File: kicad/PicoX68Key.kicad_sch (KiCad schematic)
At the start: 20 parts, among them J1 TO_X68000, Q1 2N7000, Q2 2N7000, Q3 2N7000, U1 Pico

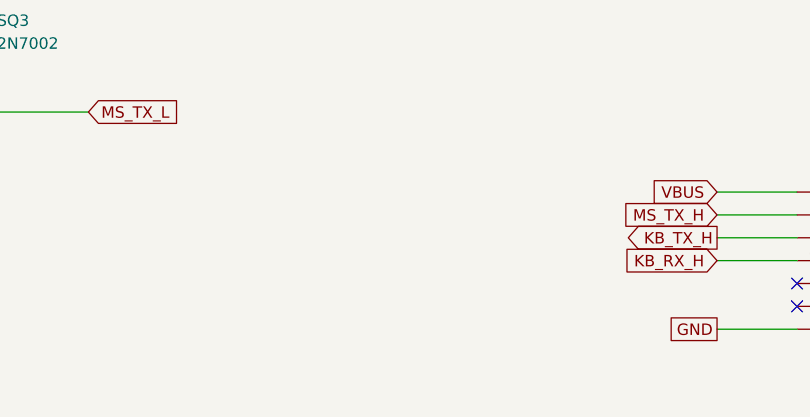
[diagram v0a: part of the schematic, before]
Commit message: Add mini-din7 connector, finish routing
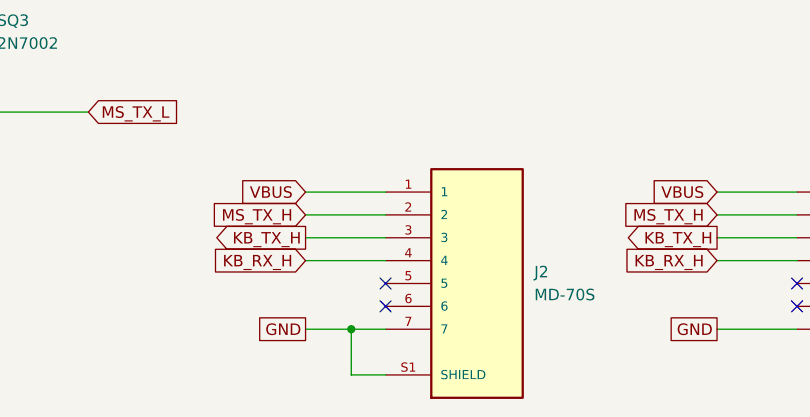
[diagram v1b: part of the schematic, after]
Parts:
- added J2: MD-70S, Library:CUI_MD-70S, symbol Library:MD-70S
- J1: footprint Connector_PinSocket_2.54mm:PinSocket_1x07_P2.54mm_Horizontal -> Connector_PinSocket_2.54mm:PinSocket_1x07_P2.54mm_Vertical
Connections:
- net GND: now also J2.7, J2.S1 (SHIELD)
- net KB_RX_H: now also J2.4
- net KB_TX_H: now also J2.3
- net MS_TX_H: now also J2.2
- net VBUS: now also J2.1
- no-connect marks 30 -> 32

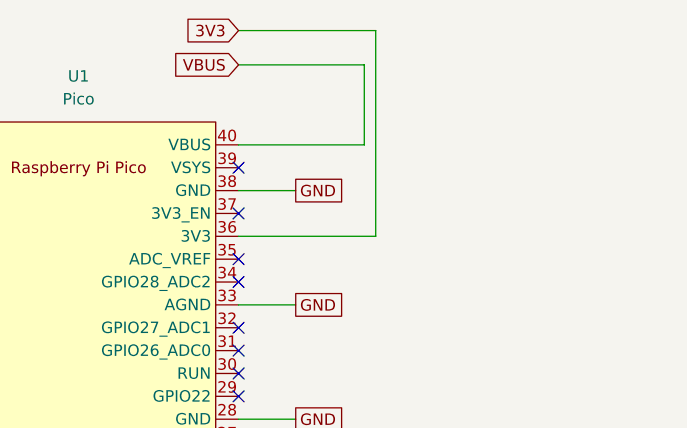
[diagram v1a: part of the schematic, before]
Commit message: Layout tidy up, add flood planes
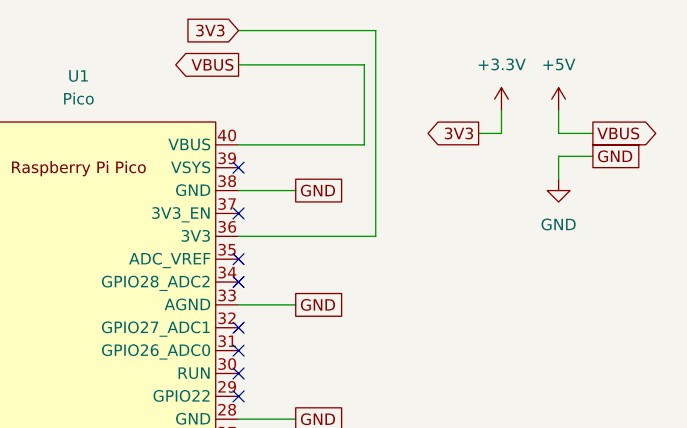
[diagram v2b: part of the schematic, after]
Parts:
- Q1, Q2, Q3: footprint Package_TO_SOT_THT:TO-92_Inline -> Package_TO_SOT_THT:TO-92L_Inline_Wide
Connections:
- net 3V3 renamed +3.3V
- net VBUS renamed +5V

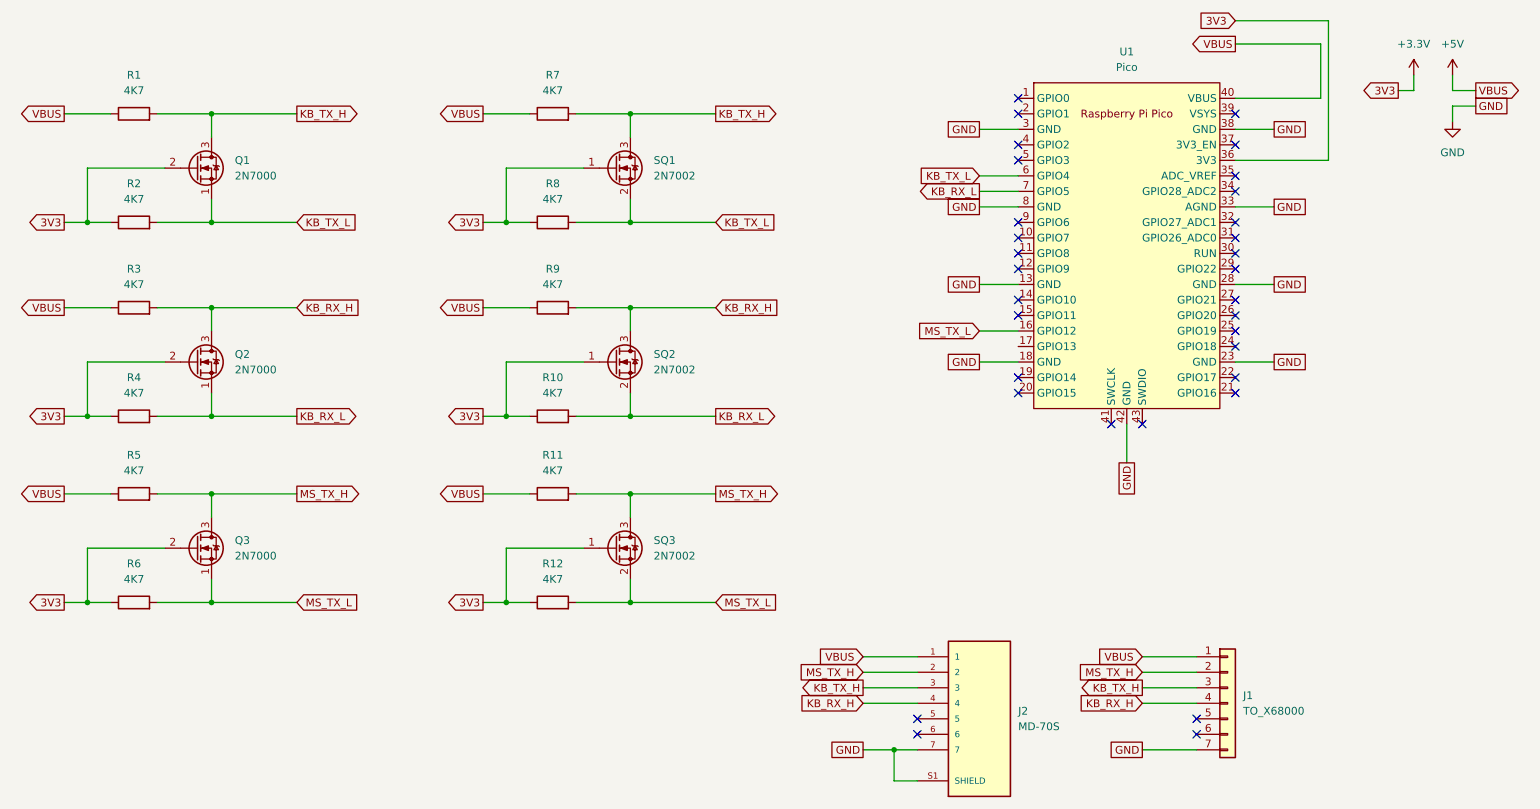
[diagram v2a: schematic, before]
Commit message: New Pico footprint, change pin header to be SPI for future LED board
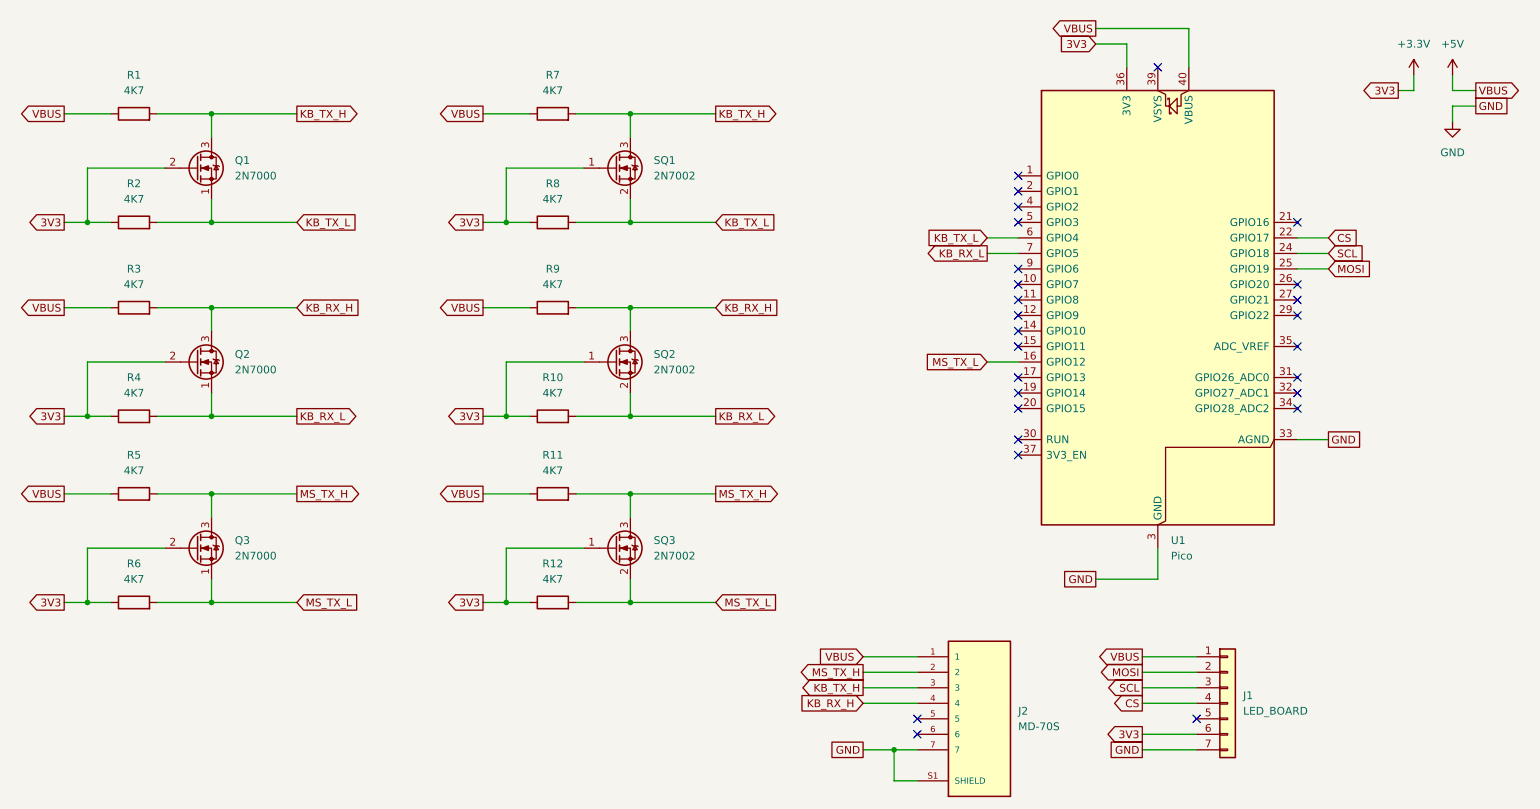
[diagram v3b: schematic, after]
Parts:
- J1: value TO_X68000 -> LED_BOARD
- U1: footprint MCU_RaspberryPi_and_Boards:RPi_Pico_SMD_TH -> Module_RaspberryPi_Pico:RaspberryPi_Pico_Common; symbol Library:Pico -> Library:RaspberryPi_Pico
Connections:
- net +3.3V: now also J1.6 (Pin_6)
- net GND: no longer U1.42 (GND)
- net KB_RX_H: no longer J1.4 (Pin_4)
- net KB_TX_H: no longer J1.3 (Pin_3)
- net MS_TX_H: no longer J1.2 (Pin_2)
- net CS: now reaches U1.22 (GPIO17)
- net CS: now also J1.4 (Pin_4)
- net SCL: now reaches U1.24 (GPIO18)
- net SCL: now also J1.3 (Pin_3)
- net MOSI: now reaches U1.25 (GPIO19)
- net MOSI: now also J1.2 (Pin_2)
- no-connect marks 32 -> 27

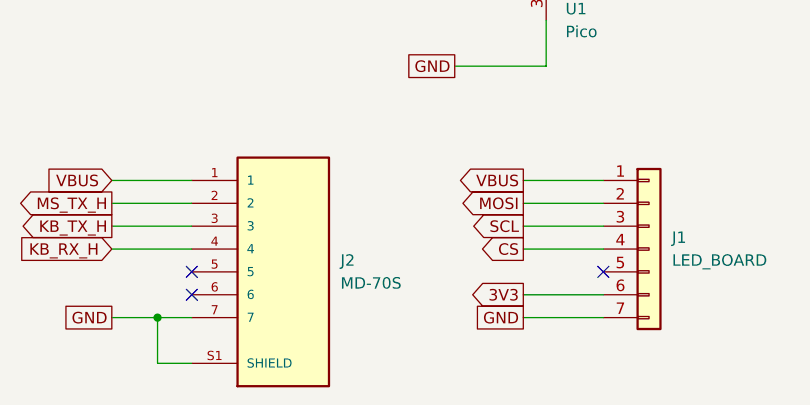
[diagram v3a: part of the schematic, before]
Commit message: Fix DIN footprint, board cleanup, silkscreen shenanigans
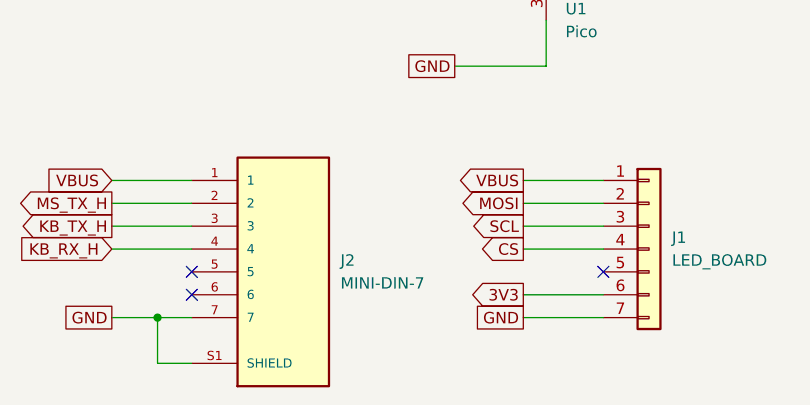
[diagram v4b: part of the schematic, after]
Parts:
- J2: value MD-70S -> MINI-DIN-7; footprint Library:CUI_MD-70S -> Library:Mini_DIN_round_7_canned
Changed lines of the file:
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@@
 			)
 		)
-		(property "Value" "MD-70S"
+		(property "Value" "MINI-DIN-7"
 			(at 194.31 132.0799 0)
 			(effects
@@
 			)
 		)
-		(property "Footprint" "Library:CUI_MD-70S"
+		(property "Footprint" "Library:Mini_DIN_round_7_canned"
 			(at 187.96 130.81 0)
 			(effects
